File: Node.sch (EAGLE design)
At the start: 67 parts, among them J1 AVR_SPI_PRG_6NS, J2 M04X2, Q1 PMR280UN, Q2 PMR280UN, Q3 PMR280UN, SW1 KSS, SW2 KSS, U1 ATMEGA32U4QFN, U2 BLUETOOTH-RN41", U3 LSM303DLM, U4 L3GD20, U5 8.0MHz, U6 MCP73871, U7 V_REG_LDOSMD, U9 RCLAMP0502A, X1 USBSMD

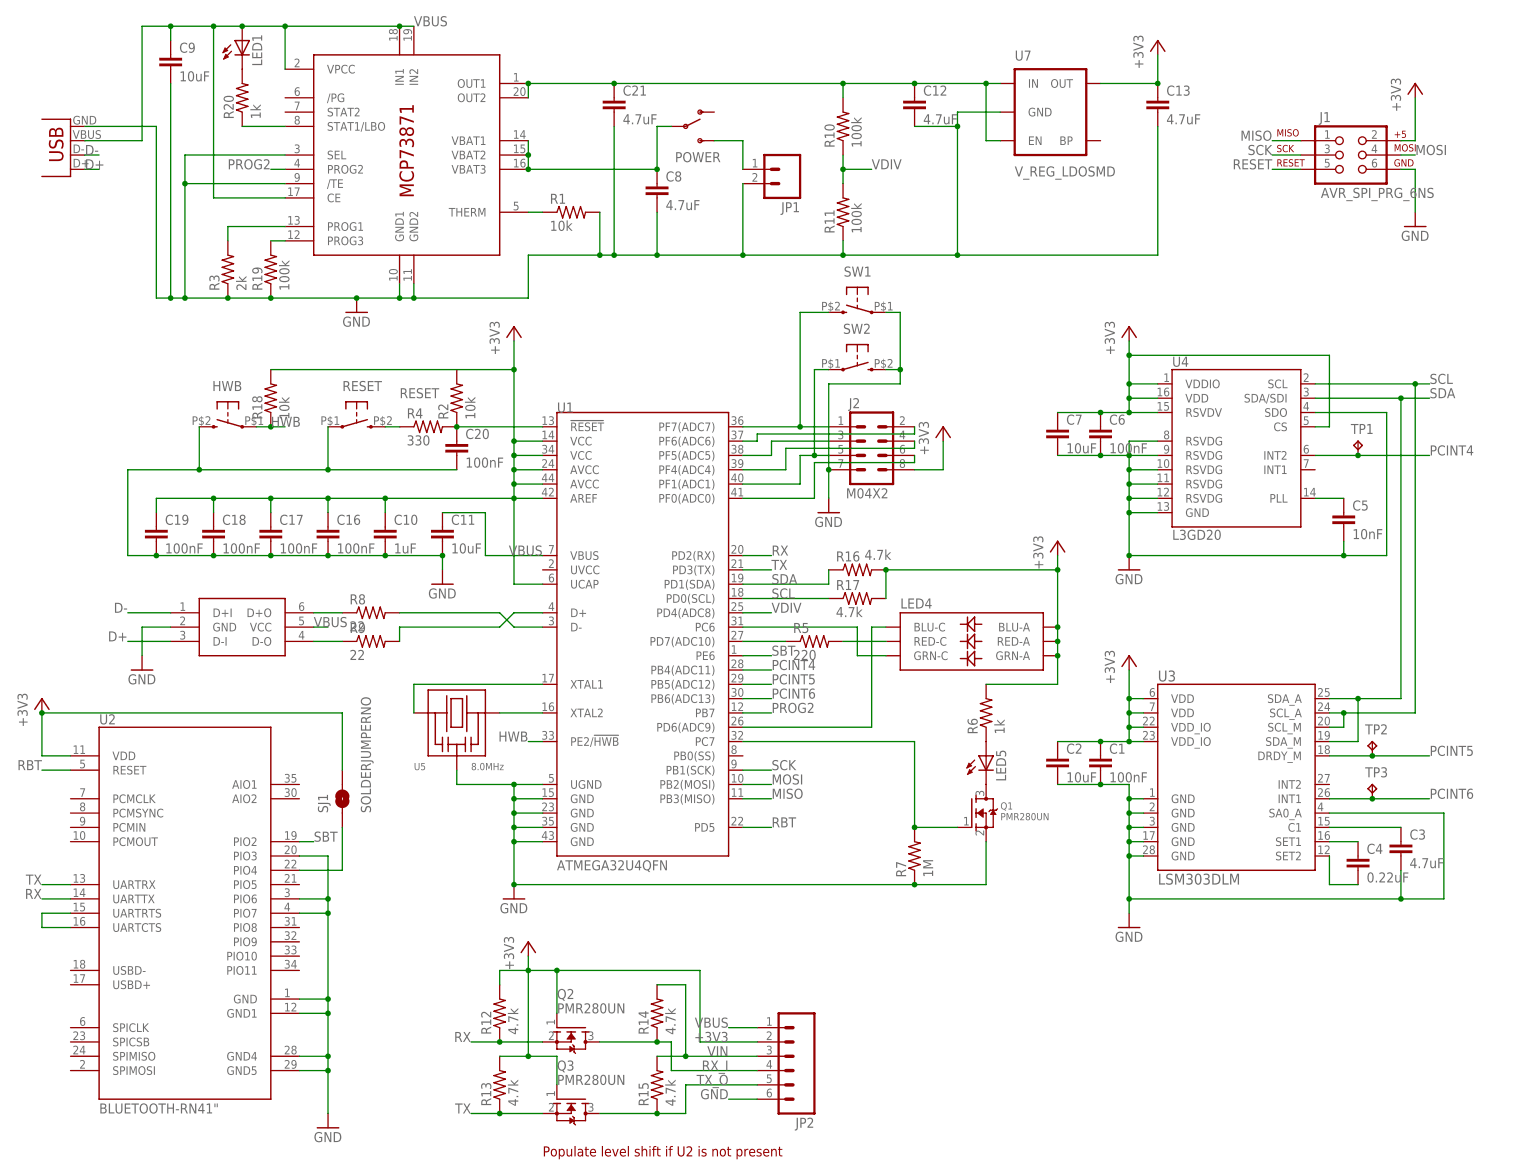
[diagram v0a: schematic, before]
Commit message: starting rev 2, using LTC3554
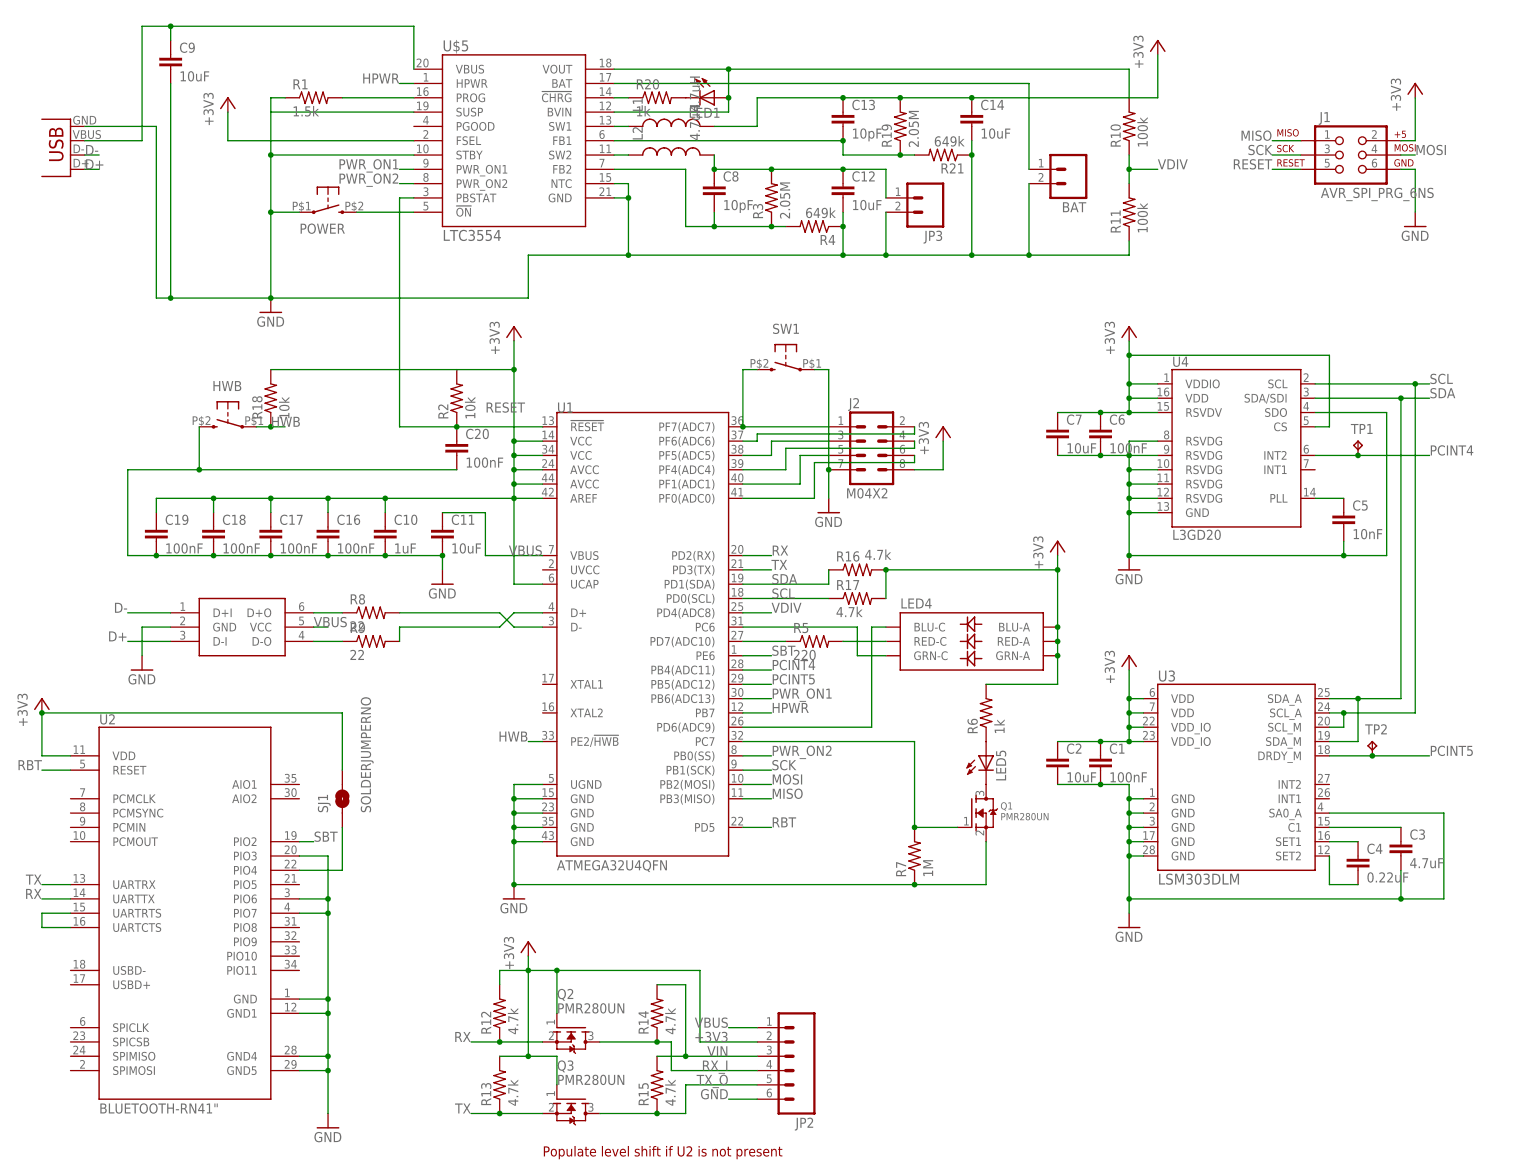
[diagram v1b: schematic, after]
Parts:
- removed C21: 4.7uF, SparkFun:CAP0603-CAP
- removed JP1: (no value), SparkFun:M02-JST-2MM-SMT
- removed RESET, SW2: KSS, adjacent-reality:KSS
- removed TP3: TPTP06R, testpad:TPTP06R
- removed U5: 8.0MHz, adjacent-reality:RESONATOR
- removed U6: MCP73871, adafruit:MCP73871
- removed U7: V_REG_LDOSMD, SparkFun:V_REG_LDOSMD
- added BAT: (no value), SparkFun:M02-JST-2MM-SMT
- added C14: 10uF, SparkFun:CAP0603-CAP
- added JP3: (no value), SparkFun-Connectors:M02PTH
- added L1, L2: 4.7uH, SparkFun-Passives:INDUCTOR1210
- added R21: 649k, SparkFun:RESISTOR0402-RES
- added U$5: LTC3554, adjacent-reality:LTC3554
- C12: value 4.7uF -> 10uF
- C13, C8: value 4.7uF -> 10pF; device SparkFun:CAP0603-CAP -> SparkFun:CAP0402-CAP
- POWER: value (none) -> KSS; device SparkFun:SWITCH-SPST-SMD-A -> adjacent-reality:KSS
- R1: value 10k -> 1.5k
- R19: value 100k -> 2.05M
- R3: value 2k -> 2.05M
- R4: value 330 -> 649k
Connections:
- removed net N$11: C12.1, C21.1, R10.2, U6.OUT1, U6.OUT2, U7.EN, U7.IN
- removed net N$36: R19.2, U6.PROG3
- removed net N$4: C8.1, POWER.P, U6.VBAT1, U6.VBAT2, U6.VBAT3
- removed net PCINT6: TP3.TP, U1.PB6(ADC13), U3.INT1
- removed net PROG2: U1.PB7, U6.PROG2
- new net HPWR: U$5.HPWR, U1.PB7
- new net N$23: L2.1, U$5.SW2
- new net N$31: C8.2, R3.1, R4.2, U$5.FB2
- new net N$37: C13.2, R19.1, R21.2, U$5.FB1
- new net PWR_ON1: U$5.PWR_ON1, U1.PB6(ADC13)
- new net PWR_ON2: U$5.PWR_ON2, U1.PB0(SS)
- net +3V3: now also C14.1, L1.2, R19.2, U$5.FSEL; no longer U7.OUT
- net GND: now also BAT.2, C14.2, JP3.2, POWER.1, R1.1, R21.1, R4.1, U$5.GND, U$5.NTC, U$5.STBY, U$5.SUSP; no longer C13.2, C21.2, C8.2, JP1.2, R1.2, R19.1, R3.1, RESET.1, SW2.3, U5.GND, U6./TE, U6.GND1, U6.GND2, U6.SEL, U7.GND
- net N$1: now also LED1.A, R10.2, U$5.BVIN, U$5.VOUT; no longer U1.XTAL2, U5.2
- net N$16: now also R20.1, U$5.!CHRG; no longer R3.2, U6.PROG1
- net N$19: now also C12.1, C8.1, JP3.1, L2.2, R3.2; no longer R20.1, U6.STAT1/LBO
- net N$2: now also R1.2, U$5.PROG; no longer U1.XTAL1, U5.1
- net N$27: now also L1.1, U$5.SW1; no longer C20.1, R2.1, R4.2, U1.!RESET
- net N$29: now also BAT.1, U$5.BAT; no longer JP1.1, POWER.S
- net N$34: no longer SW2.1
- net N$8: now also POWER.3, U$5.!ON; no longer R1.1, U6.THERM
- net RESET: now also C20.1, R2.1, U$5.PBSTAT, U1.!RESET; no longer R4.1, RESET.3
- net VBUS: now also U$5.VBUS; no longer LED1.A, U6.CE, U6.IN1, U6.IN2, U6.VPCC
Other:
- moved on the sheet: C12, C13, C8, LED1, R1, R10, R11, R19, R20, R3, R4, SW1

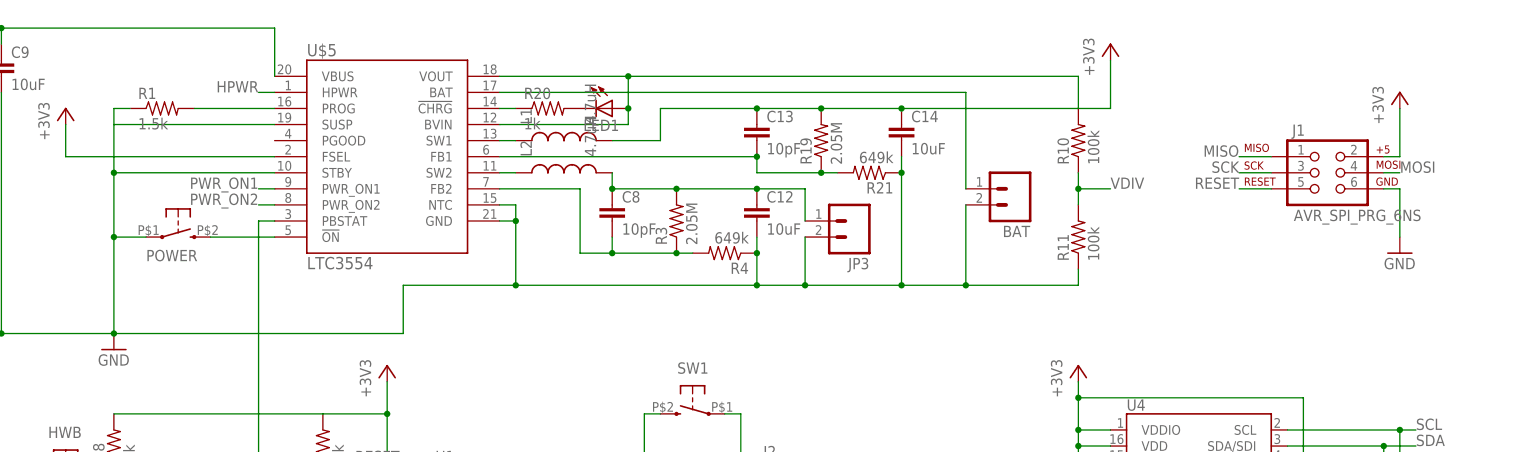
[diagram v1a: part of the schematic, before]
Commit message: properly decouple LTC3554
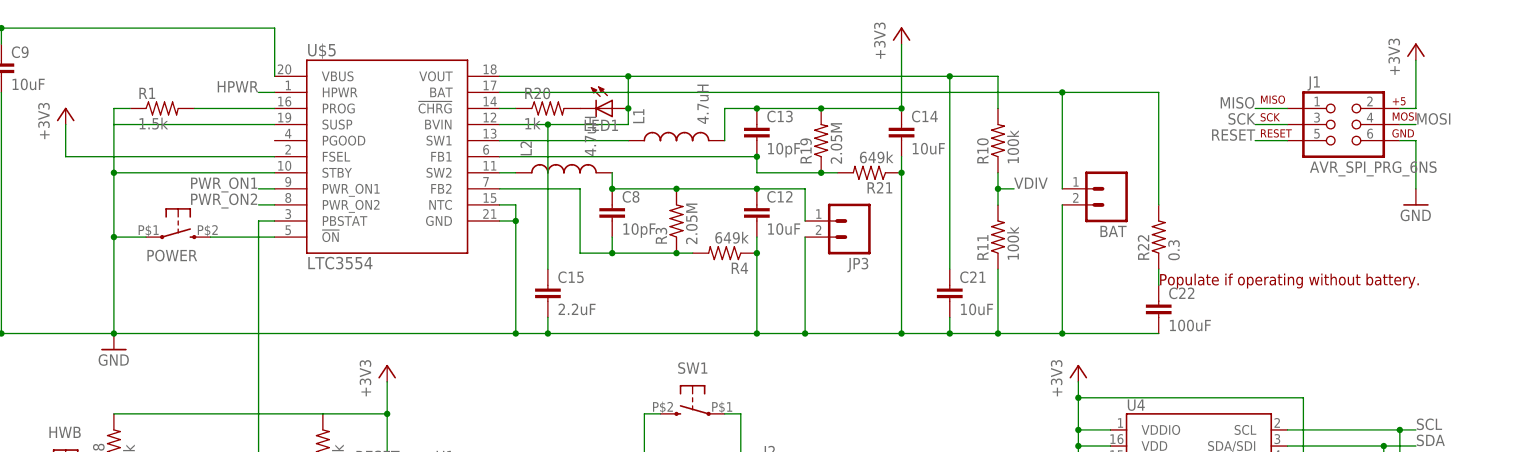
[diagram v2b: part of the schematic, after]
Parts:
- added C15: 2.2uF, SparkFun:CAP0402-CAP
- added C21: 10uF, SparkFun:CAP0402-CAP
- added C22: 100uF, SparkFun:CAP1210
- added R22: 0.3, SparkFun:RESISTOR0603-RES
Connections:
- new net N$36: C22.1, R22.1
- net GND: now also C15.2, C21.2, C22.2
- net N$1: now also C15.1, C21.1
- net N$29: now also R22.2
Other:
- note added: "Populate if operating without battery."
- moved on the sheet: BAT, J1, L1, R10, R11

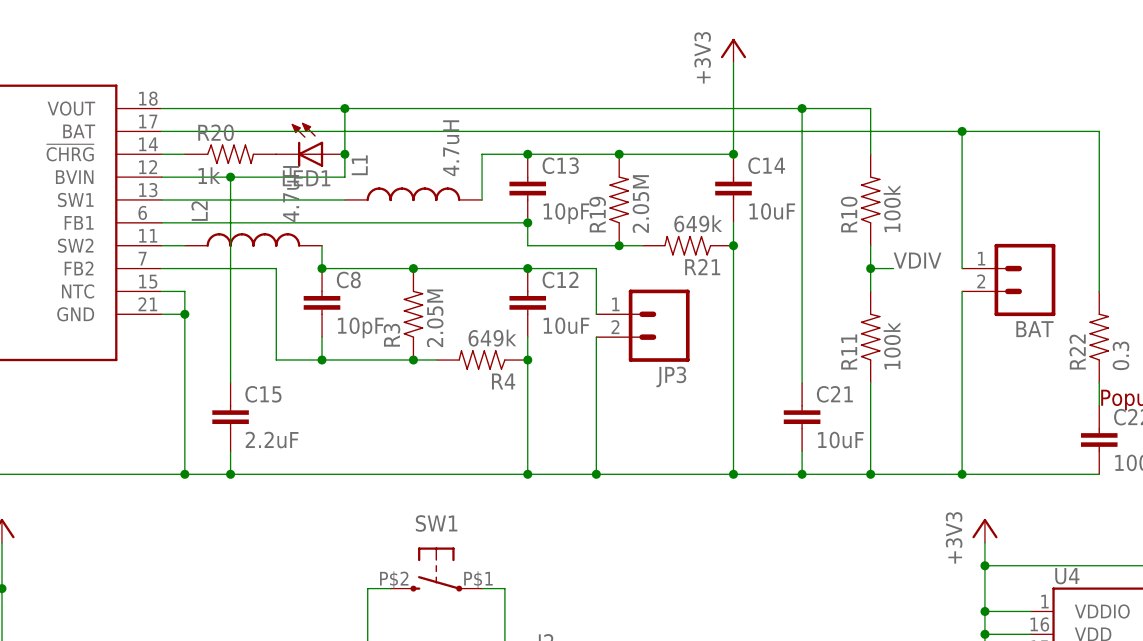
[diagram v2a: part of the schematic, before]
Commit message: and one more 1uF for the battery
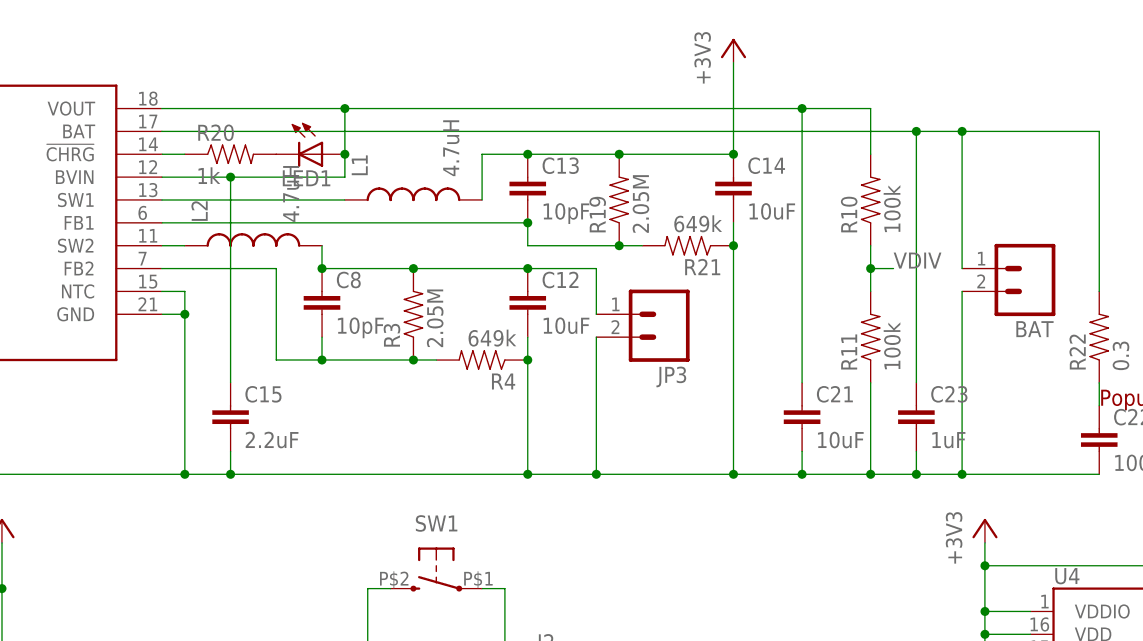
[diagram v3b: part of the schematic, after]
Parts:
- added C23: 1uF, SparkFun:CAP0402-CAP
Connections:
- net GND: now also C23.2
- net N$29: now also C23.1
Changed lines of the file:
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@@
 <part name="R22" library="SparkFun" deviceset="RESISTOR" device="0603-RES" value="0.3"/>
 <part name="C22" library="SparkFun" deviceset="CAP" device="1210" value="100uF"/>
+<part name="C23" library="SparkFun" deviceset="CAP" device="0402-CAP" value="1uF"/>
 </parts>
 <sheets>
@@
 <instance part="R22" gate="G$1" x="220.98" y="172.72" rot="R90"/>
 <instance part="C22" gate="G$1" x="220.98" y="160.02"/>
+<instance part="C23" gate="G$1" x="200.66" y="162.56"/>
 </instances>
 <busses>
@@
 <pinref part="BAT" gate="G$1" pin="2"/>
 <wire x1="205.74" y1="177.8" x2="205.74" y2="157.48" width="0.1524" layer="91"/>
-<wire x1="195.58" y1="157.48" x2="205.74" y2="157.48" width="0.1524" layer="91"/>
+<wire x1="195.58" y1="157.48" x2="200.66" y2="157.48" width="0.1524" layer="91"/>
 <junction x="195.58" y="157.48"/>
 <pinref part="C22" gate="G$1" pin="2"/>
+<wire x1="200.66" y1="157.48" x2="205.74" y2="157.48" width="0.1524" layer="91"/>
 <wire x1="220.98" y1="157.48" x2="205.74" y2="157.48" width="0.1524" layer="91"/>
 <junction x="205.74" y="157.48"/>
+<pinref part="C23" gate="G$1" pin="2"/>
+<wire x1="200.66" y1="160.02" x2="200.66" y2="157.48" width="0.1524" layer="91"/>
+<junction x="200.66" y="157.48"/>
 </segment>
 <segment>
@@
 <pinref part="BAT" gate="G$1" pin="1"/>
 <pinref part="U$5" gate="G$1" pin="BAT"/>
-<wire x1="116.84" y1="195.58" x2="205.74" y2="195.58" width="0.1524" layer="91"/>
+<wire x1="116.84" y1="195.58" x2="200.66" y2="195.58" width="0.1524" layer="91"/>
+<wire x1="200.66" y1="195.58" x2="205.74" y2="195.58" width="0.1524" layer="91"/>
 <wire x1="205.74" y1="195.58" x2="205.74" y2="180.34" width="0.1524" layer="91"/>
 <pinref part="R22" gate="G$1" pin="2"/>
@@
 <wire x1="220.98" y1="195.58" x2="220.98" y2="177.8" width="0.1524" layer="91"/>
 <junction x="205.74" y="195.58"/>
-</segment>
-</net>
+<pinref part="C23" gate="G$1" pin="1"/>
+<wire x1="200.66" y1="167.64" x2="200.66" y2="195.58" width="0.1524" layer="91"/>
+<junction x="200.66" y="195.58"/>
+</segment>
+</net>
